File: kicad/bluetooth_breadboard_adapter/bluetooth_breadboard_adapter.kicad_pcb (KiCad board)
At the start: 2 copper layers, 26.9 x 39.6 mm, 4 parts, among them J1 SCJ368R1NUS0B00G, P1 CONNECTOR, P2 CONNECTOR, U1 BLK-MD-SPK-B

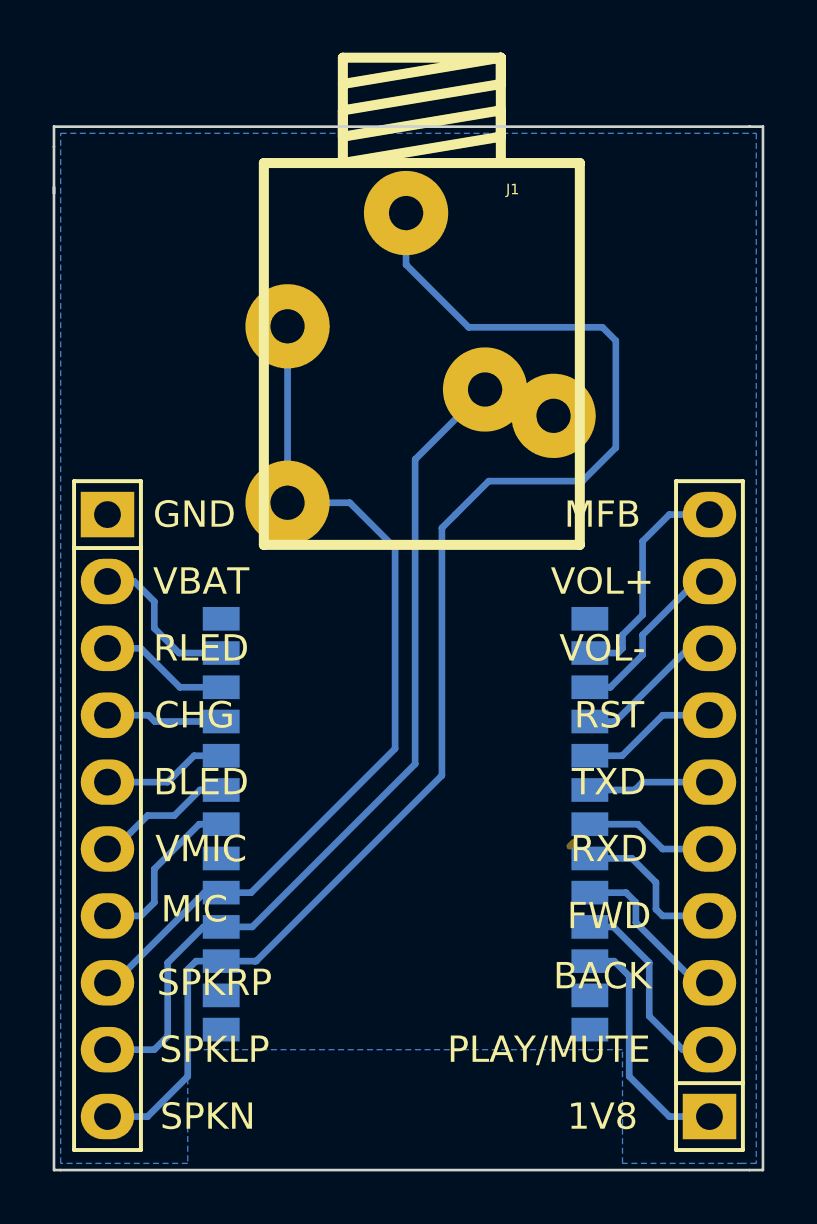
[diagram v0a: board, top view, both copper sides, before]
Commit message: smaller 2layers board
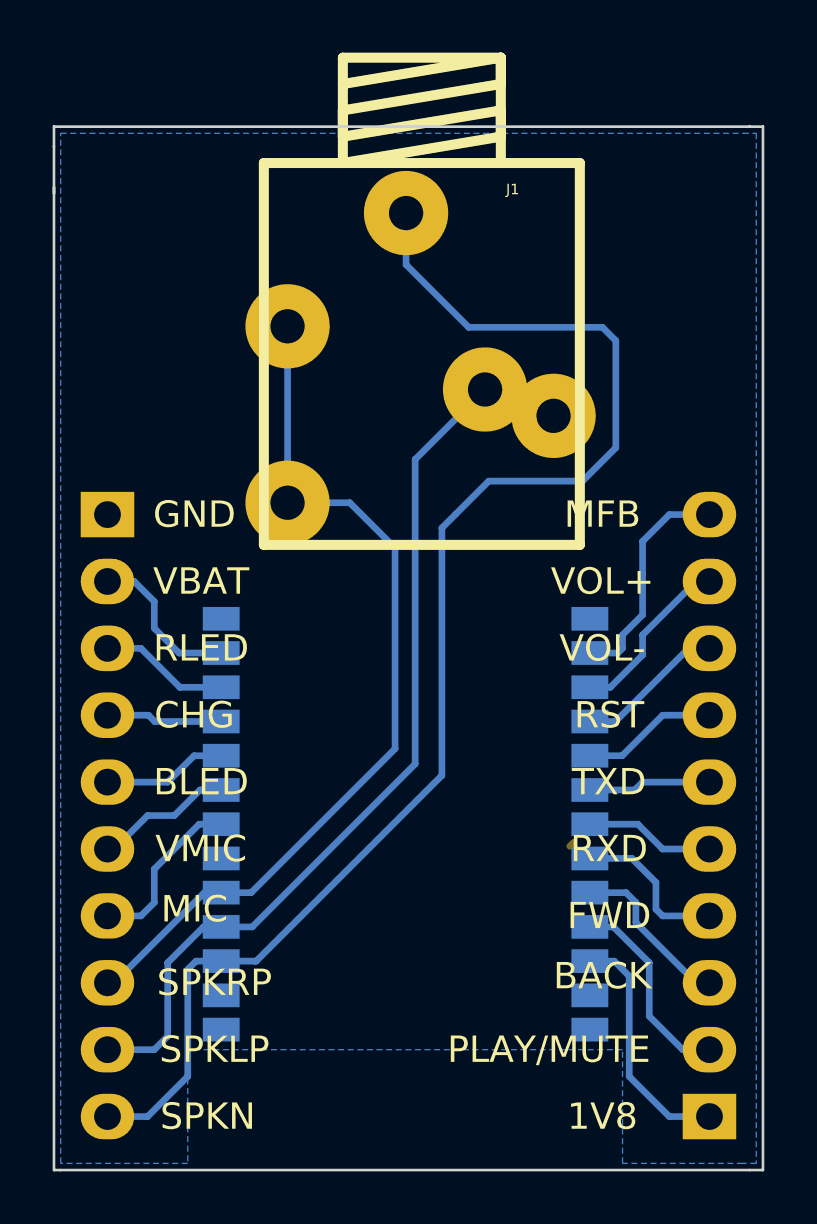
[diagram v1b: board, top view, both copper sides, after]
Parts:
- P1, P2: footprint Socket_Strips:Socket_Strip_Straight_1x10 -> Pin_Headers:Pin_Header_Straight_1x10; moved to B.Cu
- turned P1 to 90 degrees
- turned P2 to 270 degrees

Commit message: geber export, OSHW logo
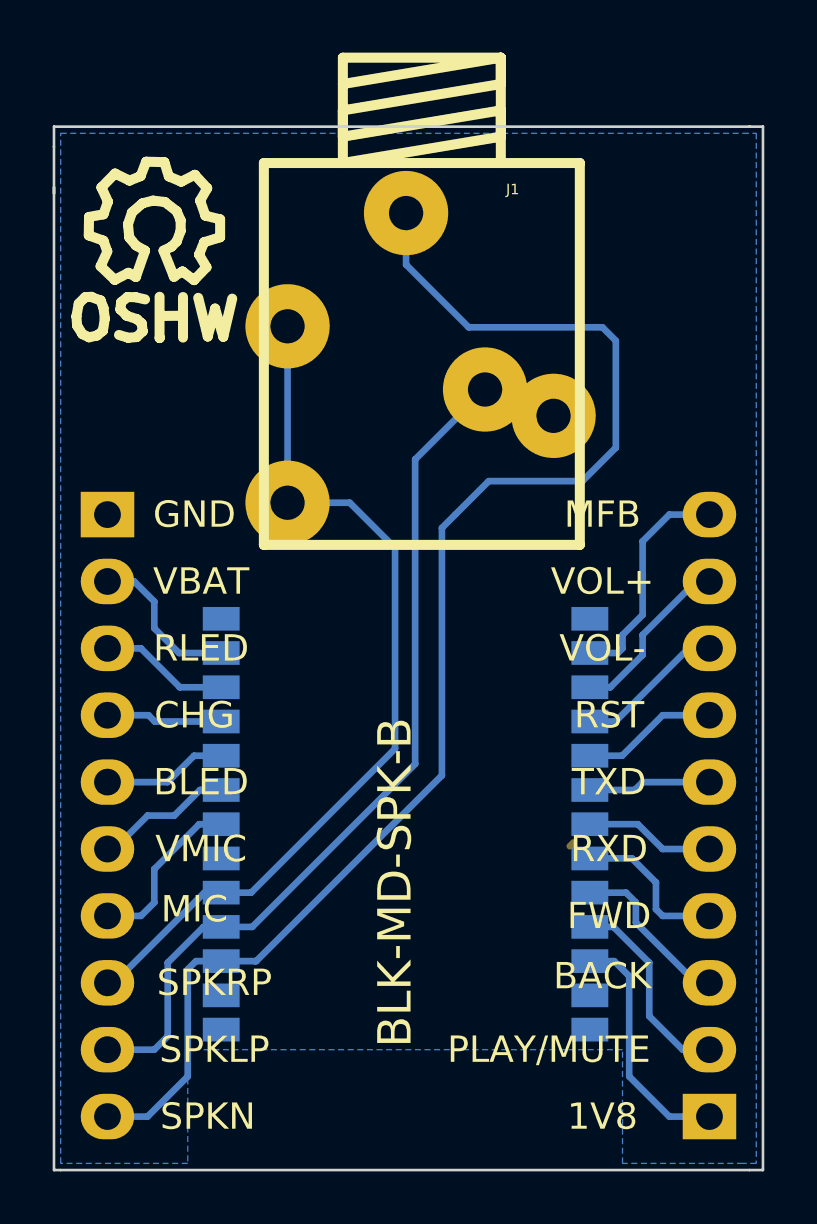
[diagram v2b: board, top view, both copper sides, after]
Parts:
- added SYM: Symbol_OSHW-Logo_SilkScreen_07Jul2012, Symbols:Symbol_OSHW-Logo_SilkScreen, F.Cu at (211.6, 132.8)
- U1: footprint BLK-MD-SPK-B.mod:BLK-MD-SPK-B -> BLK-MD-SPK-B:BLK-MD-SPK-B

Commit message: update patch to modules becouse of changed library name
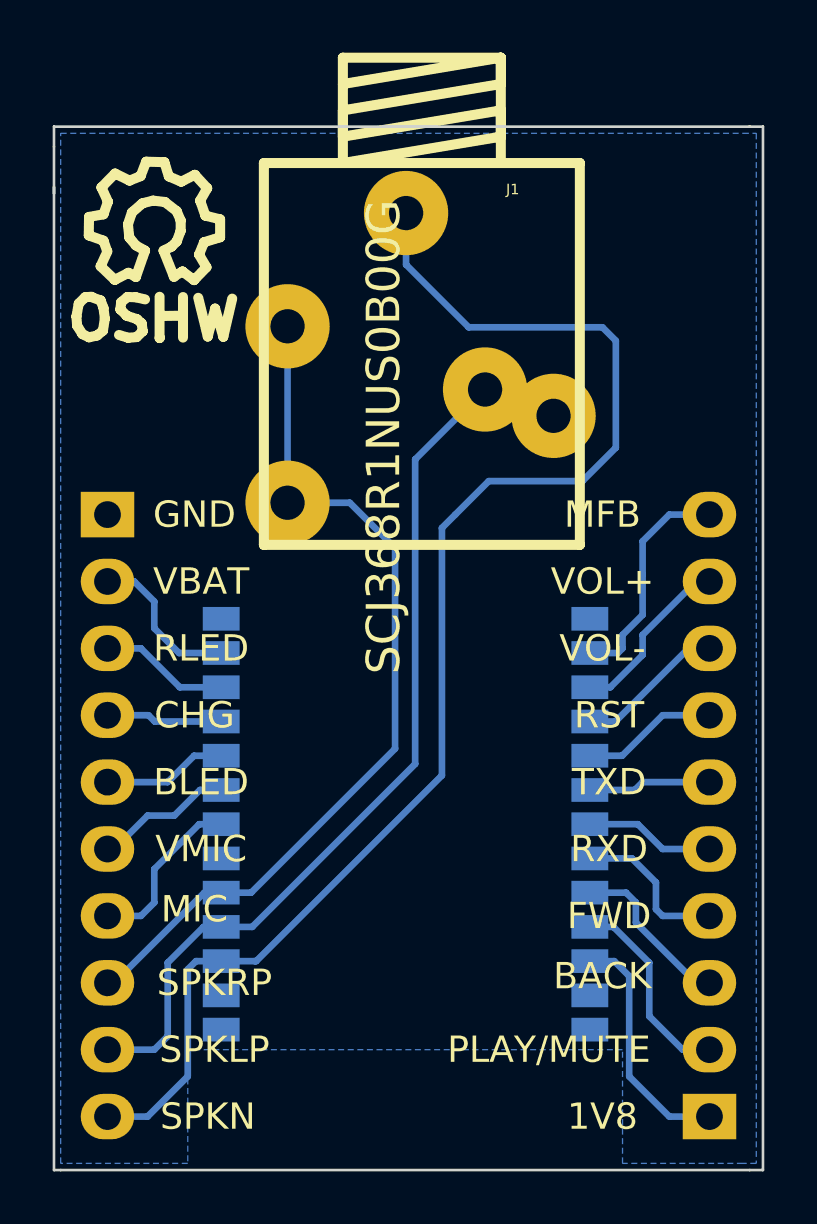
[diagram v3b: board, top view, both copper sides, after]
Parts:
- J1: footprint 3.5mm stereo jack:3.5mm_stereo_jack -> my_modules:3.5mm_stereo_jack
- U1: footprint BLK-MD-SPK-B:BLK-MD-SPK-B -> my_modules:BLK-MD-SPK-B

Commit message: bluetooth board update
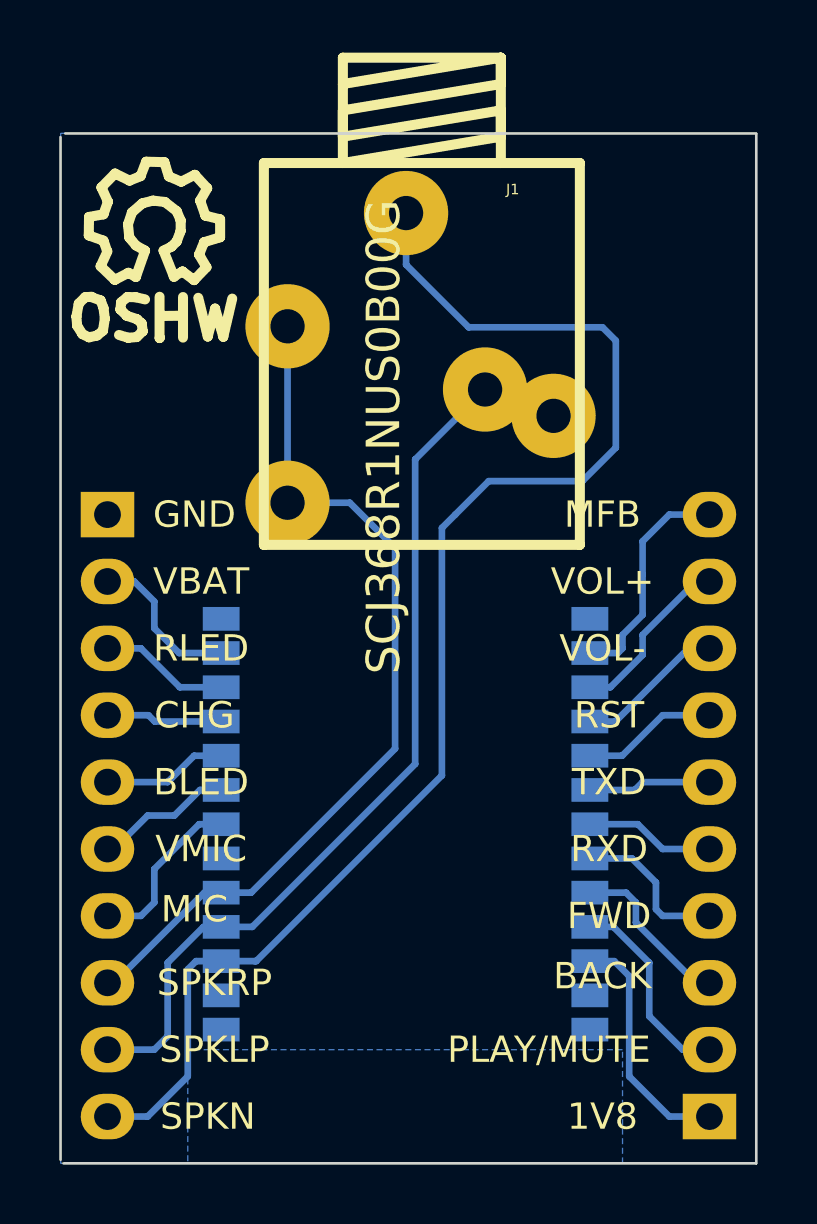
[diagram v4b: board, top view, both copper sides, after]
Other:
- board size 26.9 x 39.6 mm -> 26.4 x 39.1 mm

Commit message: 3.5mm jack update to scj-0354-5PU
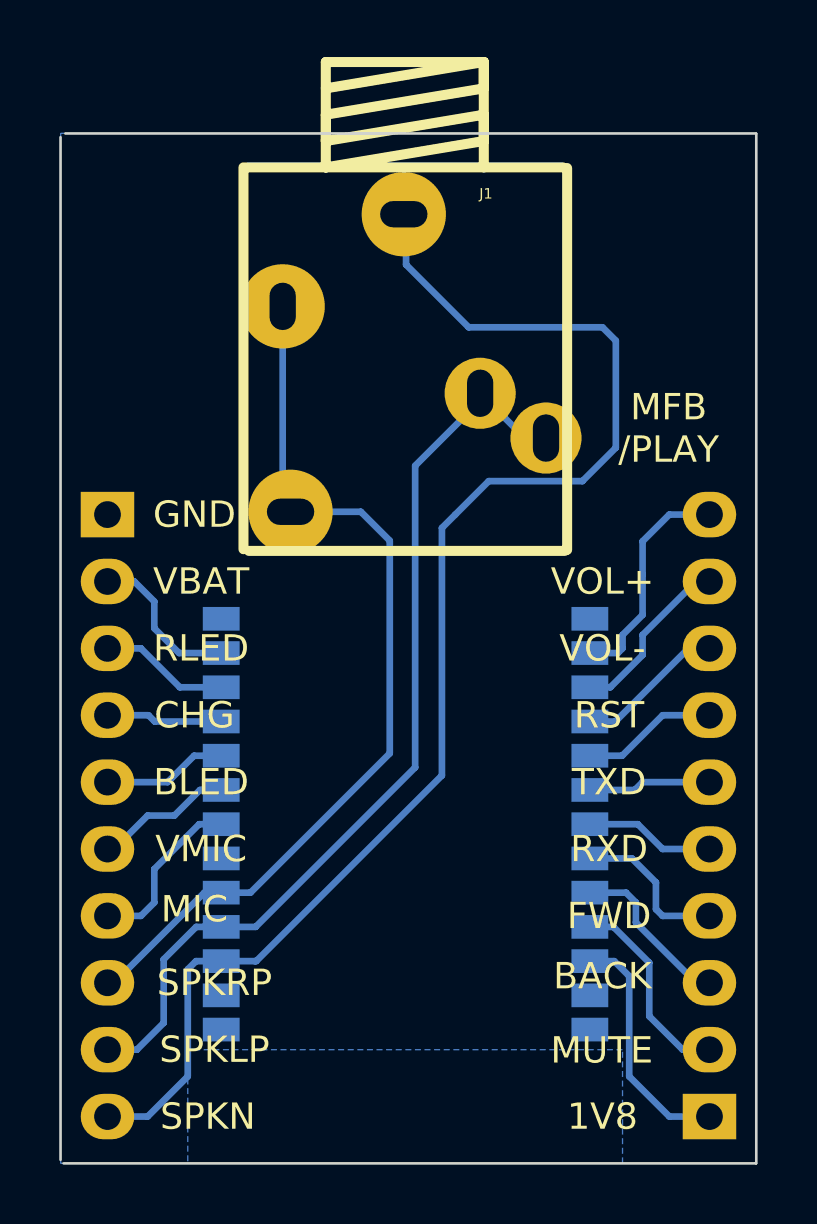
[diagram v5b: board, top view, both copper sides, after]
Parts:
- removed SYM: Symbol_OSHW-Logo_SilkScreen_07Jul2012, Symbols:Symbol_OSHW-Logo_SilkScreen
- J1: value SCJ368R1NUS0B00G -> SCJ-0354-5PU; footprint my_modules:3.5mm_stereo_jack -> jacks:SCJ-0354-5PU
- moved J1 6.79 mm to (221.1, 130.7)
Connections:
- P2 pad 8: Net-(J1-Pad2) -> Net-(J1-Pad4)
- P2 pad 9: Net-(J1-Pad4) -> Net-(J1-Pad2)
- U1 pad 4: Net-(J1-Pad4) -> Net-(J1-Pad2)
- U1 pad 5: Net-(J1-Pad2) -> Net-(J1-Pad4)
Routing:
- net Net-(J1-Pad2): track 34.2 -> 37.3 mm
- net Net-(J1-Pad4): track 37.2 -> 34.7 mm
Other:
- board text added: "MFB /PLAY"
- board text added: "MUTE"
- board text removed: "MFB"
- board text removed: "PLAY/MUTE"
